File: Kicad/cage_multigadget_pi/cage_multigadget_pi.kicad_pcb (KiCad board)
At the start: 2 copper layers, 0.7 x 2.2 mm, 41 parts, among them J1 USB_B_Micro, J2 Raspberry_Pi_2_3, Q1 BSN20, Q2 BSN20, Q3 BSN20, Q4 BSN20, Q5 BSN20, U1 OP495, U2 MCP3004, U3 LED_shift_register_SPI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

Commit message: Updating the edges of the boards
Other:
- board size 0.7 x 2.2 mm -> 54.3 x 107.2 mm
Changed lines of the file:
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@@
-(kicad_pcb (version 20171130) (host pcbnew 5.1.4-e60b266~84~ubuntu18.04.1)
+(kicad_pcb (version 20171130) (host pcbnew 5.1.5-52549c5~84~ubuntu18.04.1)
   (general
     (thickness 1.6)
-    (drawings 3)
+    (drawings 7)
     (tracks 435)
     (zones 0)
@@
     )
   )
+  (gr_line (start 170.8531 51.6001) (end 116.5987 51.6001) (layer Edge.Cuts) (width 0.1))
+  (gr_line (start 170.8531 158.7881) (end 170.8531 51.6001) (layer Edge.Cuts) (width 0.1))
+  (gr_line (start 116.586 158.7881) (end 170.8531 158.7881) (layer Edge.Cuts) (width 0.1))
+  (gr_line (start 116.586 51.6001) (end 116.586 158.7881) (layer Edge.Cuts) (width 0.1))
   (gr_text "MULTIGADGET DEVICES" (at 153.6 140.3 90) (layer F.SilkS)
     (effects (font (size 1.5 1.5) (thickness 0.3)))
@@
   (segment (start 141.8 65.67863) (end 138.811372 62.690002) (width 0.25) (layer F.Cu) (net 11))
   (segment (start 141.8 66.81) (end 141.8 65.67863) (width 0.25) (layer F.Cu) (net 11))
-  (segment (start 122.559001 56.435001) (end 127.9906 61.8666) (width 0.25) (layer B.Cu) (net 43))
-  (segment (start 121.459001 56.435001) (end 122.559001 56.435001) (width 0.25) (layer B.Cu) (net 43) (status 10))
-  (via (at 127.9906 135.7249) (size 0.8) (drill 0.4) (layers F.Cu B.Cu) (net 43))
   (segment (start 121.506002 79.248) (end 121.459001 79.295001) (width 0.25) (layer F.Cu) (net 23) (status 30))
   (segment (start 126.311 79.248) (end 121.506002 79.248) (width 0.25) (layer F.Cu) (net 23) (status 30))
@@
   (segment (start 126.057 124.245) (end 126.558 124.746) (width 0.25) (layer F.Cu) (net 27) (status 20))
   (segment (start 126.057 121.158) (end 126.057 124.245) (width 0.25) (layer F.Cu) (net 27) (status 10))
+  (segment (start 122.559001 56.435001) (end 127.9906 61.8666) (width 0.25) (layer B.Cu) (net 43))
+  (segment (start 121.459001 56.435001) (end 122.559001 56.435001) (width 0.25) (layer B.Cu) (net 43) (status 10))
+  (via (at 127.9906 135.7249) (size 0.8) (drill 0.4) (layers F.Cu B.Cu) (net 43))
   (segment (start 129.286 82.246) (end 128.712 82.82) (width 0.25) (layer F.Cu) (net 43) (status 20))
   (segment (start 129.286 79.248) (end 129.286 82.246) (width 0.25) (layer F.Cu) (net 43) (status 10))

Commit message: added reward line, changed 2x40 pin header to 2x20 header, changed USB footprint and shifted
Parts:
- added J3: Reward, Socket_Strips:Socket_Strip_Straight_1x02_Pitch2.54mm, F.Cu at (143.5, 54.6)
- J1: footprint Connector_USB:USB_Micro-B_Amphenol_10103594-0001LF_Horizontal -> Digikey_footprints:USB_Micro_B_Female_10118194-0001LF
- J2: footprint Connector_PinSocket_2.54mm:PinSocket_2x40_P2.54mm_Vertical -> Pin_Headers:Pin_Header_Straight_2x20_Pitch2.54mm; moved to B.Cu
- moved J1 0.36 mm to (130.8, 57.1)
- moved J2 0.07 mm to (121.4, 56.4), turned to 180 degrees
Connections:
- J2 pad 11: Net-(J2-Pad11) -> /Reward
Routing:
- net /Reward: track 0.00 -> 38.7 mm
- net GND: track 181.4 -> 201.1 mm
- net Net-(J1-Pad6): track 10.6 -> 0.00 mm
- net +5V: track 278.4 -> 280.1 mm

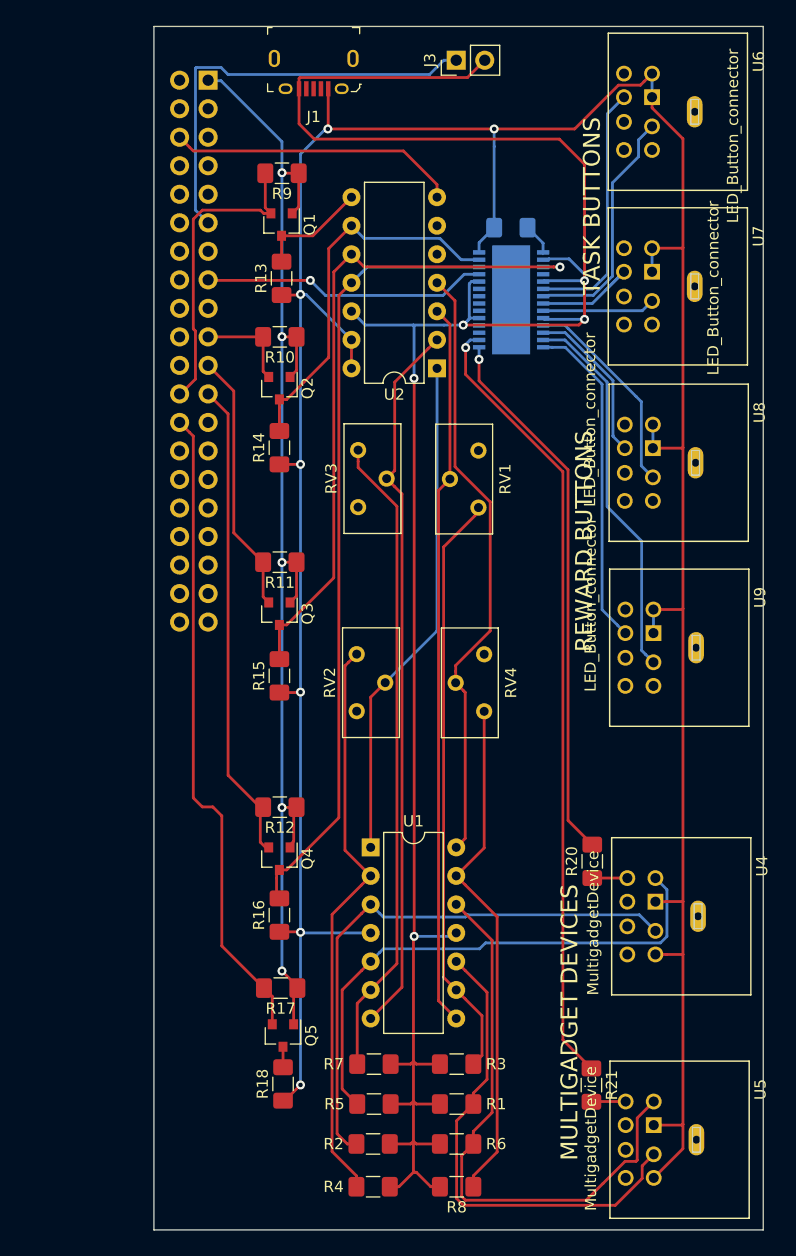
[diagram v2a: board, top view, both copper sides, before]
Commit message: changes to the multigadget circuit
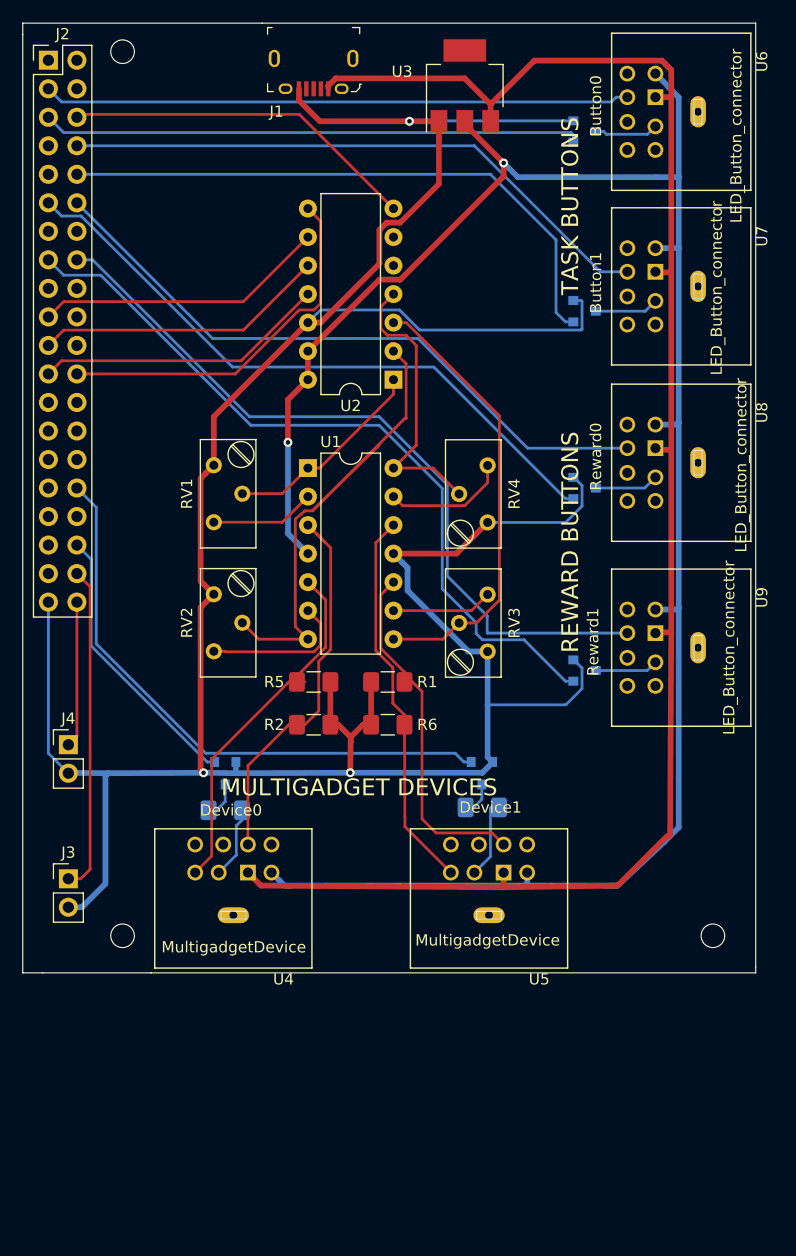
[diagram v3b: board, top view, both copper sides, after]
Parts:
- removed R10, R11, R12, R13, R14, R15, R16, R17, R18, R19, R9: 10k, Resistor_SMD:R_1206_3216Metric_Pad1.42x1.75mm_HandSolder
- removed R3, R4, R7, R8: 1k, Resistor_SMD:R_1206_3216Metric_Pad1.42x1.75mm_HandSolder
- added J4: Conn_01x02, Socket_Strips:Socket_Strip_Straight_1x02_Pitch2.54mm, F.Cu at (109.0, 115.6)
- added Q6: BSN20, TO_SOT_Packages_SMD:SOT-23, B.Cu at (154.9, 77.0)
- J2: moved to F.Cu
- J3: value Reward -> Conn_01x02
- Q1, Q2, Q3, Q4, Q5: footprint Package_TO_SOT_SMD:SOT-23 -> TO_SOT_Packages_SMD:SOT-23; moved to B.Cu
- R20, R21: moved to B.Cu
- RV1, RV2, RV3, RV4: footprint Potentiometer_THT:Potentiometer_Bourns_3296Y_Vertical -> Potentiometers:Potentiometer_Trimmer_Bourns_3296Y
- U3: value LED_shift_register_SPI -> AZ1117-3.3; footprint Package_SO:HTSSOP-28-1EP_4.4x9.7mm_P0.65mm_EP3.4x9.5mm_Mask2.4x6.17mm -> TO_SOT_Packages_SMD:SOT-223; moved to F.Cu
- moved Q5 84.9 mm to (154.9, 61.0), turned to 0 degrees
- moved J3 80.7 mm to (109.0, 127.5), turned to 0 degrees
- moved Q1 49.1 mm to (122.9, 118.1)
- moved Q2 38.7 mm to (145.8, 118.1)
- moved R1 38.1 mm to (137.4, 110.0)
- moved R5 38.0 mm to (130.8, 110.0)
- moved R6 37.8 mm to (137.4, 113.8)
- moved R2 37.7 mm to (130.8, 113.8)
- moved U4 36.4 mm to (125.0, 127.0), turned to 180 degrees
- moved U1 34.2 mm to (130.3, 90.9)
- moved R20 33.0 mm to (122.9, 121.4), turned to 180 degrees
- moved Q4 31.9 mm to (154.9, 109.0), turned to 0 degrees
- moved Q3 29.4 mm to (154.9, 92.7), turned to 0 degrees
- moved R21 26.6 mm to (145.8, 121.2), turned to 0 degrees
- moved U5 26.2 mm to (147.7, 127.0), turned to 180 degrees
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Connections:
- J2 pad 1: /3V_source -> Net-(J2-Pad1)
- J2 pad 10: Net-(J2-Pad10) -> /Button1LED
- J2 pad 11: /Reward -> /Reward0LED
- J2 pad 12: Net-(J2-Pad12) -> /Reward0Button
- J2 pad 15: /Reset -> /Reward1LED
- J2 pad 16: Net-(J2-Pad16) -> /Reward1Button
- J2 pad 19: /MOSI_3V -> /MOSI
- J2 pad 21: /MISO_3V -> /MISO
- J2 pad 23: /SCLK_3V -> /SCLK
- J2 pad 24: /Chip_Select_ADC_3V -> /Chip_Select_ADC
- J2 pad 26: /Chip_Select_LED_3V -> Net-(J2-Pad26)
- J2 pad 3: Net-(J2-Pad3) -> /Button0
- J2 pad 32: Net-(J2-Pad32) -> /Device1LED
- J2 pad 36: Net-(J2-Pad36) -> /Device0LED
- J2 pad 38: Net-(J2-Pad38) -> /Reward0
- J2 pad 39: Net-(J2-Pad39) -> GND
- J2 pad 40: Net-(J2-Pad40) -> /Reward1
- J2 pad 5: Net-(J2-Pad5) -> /Button0LED
- J2 pad 8: Net-(J2-Pad8) -> /Button1
- J3 pad 1: /Reward -> /Reward0
- Q1 pad 1: /3V_source -> /Device0LED
- Q1 pad 2: /Chip_Select_ADC_3V -> GND
- Q1 pad 3: /Chip_Select_ADC_5V -> Net-(Q1-Pad3)
- Q2 pad 1: /3V_source -> /Device1LED
- Q2 pad 2: /MOSI_3V -> GND
- Q2 pad 3: /MOSI_5V -> Net-(Q2-Pad3)
- Q3 pad 1: /3V_source -> /Reward0LED
- Q3 pad 2: /MISO_3V -> GND
- Q3 pad 3: /MISO_5V -> Net-(Q3-Pad3)
- Q4 pad 1: /3V_source -> /Reward1LED
- Q4 pad 2: /SCLK_3V -> GND
- Q4 pad 3: /SCLK_5V -> Net-(Q4-Pad3)
- Q5 pad 1: /3V_source -> /Button0LED
- Q5 pad 2: /Chip_Select_LED_3V -> GND
- Q5 pad 3: /Chip_Select__LED_5V -> Net-(Q5-Pad3)
- R20 pad 2: /Device0LED -> Net-(Q1-Pad3)
- R21 pad 1: /Device1LED -> Net-(Q2-Pad3)
- RV1 pad 1: Net-(R3-Pad1) -> GND
- RV2 pad 1: Net-(R4-Pad1) -> GND
- RV3 pad 1: Net-(R7-Pad1) -> GND
- RV4 pad 1: Net-(R8-Pad1) -> GND
- U1 pad 1: Net-(RV2-Pad2) -> Net-(RV1-Pad2)
- U1 pad 13: Net-(R8-Pad1) -> Net-(RV4-Pad3)
- U1 pad 2: Net-(R4-Pad1) -> Net-(RV1-Pad3)
- U1 pad 4: +5V -> +3V3
- U1 pad 6: Net-(R7-Pad1) -> Net-(RV2-Pad3)
- U1 pad 7: Net-(RV3-Pad2) -> Net-(RV2-Pad2)
- U1 pad 8: Net-(RV1-Pad2) -> Net-(RV3-Pad2)
- U1 pad 9: Net-(R3-Pad1) -> Net-(RV3-Pad3)
- U2 pad 1: Net-(RV2-Pad2) -> Net-(RV1-Pad2)
- U2 pad 10: /MISO_5V -> /MISO
- U2 pad 11: /SCLK_5V -> /SCLK
- U2 pad 13: +5V -> +3V3
- U2 pad 14: +5V -> +3V3
- U2 pad 2: Net-(RV3-Pad2) -> Net-(RV2-Pad2)
- U2 pad 3: Net-(RV1-Pad2) -> Net-(RV3-Pad2)
- U2 pad 8: /Chip_Select_ADC_5V -> /Chip_Select_ADC
- U2 pad 9: /MOSI_5V -> /MOSI
- U3 pad 1: Net-(R19-Pad2) -> GND
- U3 pad 2: GND -> +3V3
- U3 pad 3: /MISO_5V -> +5V
- U3 pad 4: /Chip_Select_LED_5V -> (no net)
- U4 pad 2: /Device0_FSR0 -> Net-(R20-Pad1)
- U4 pad 3: /Device0_FSR1 -> +3V3
- U4 pad 4: (no net) -> /Device0_FSR0
- U4 pad 5: +5V -> /Device0_FSR1
- U4 pad 6: Net-(R20-Pad1) -> (no net)
- U5 pad 2: /Device1_FSR0 -> Net-(R21-Pad2)
- U5 pad 3: /Device1_FSR1 -> +3V3
- U5 pad 4: (no net) -> /Device1_FSR0
- U5 pad 5: +5V -> /Device1_FSR1
- U5 pad 6: Net-(R21-Pad2) -> (no net)
- U6 pad 2: /ButtonLED0 -> Net-(Q5-Pad3)
- U6 pad 3: +5V -> +3V3
- U7 pad 2: /ButtonLED1 -> Net-(Q6-Pad3)
- U7 pad 3: +5V -> +3V3
- U8 pad 2: /RewardLED0 -> Net-(Q3-Pad3)
- U8 pad 3: +5V -> +3V3
- U8 pad 4: /RewardButton0 -> /Reward0Button
- U9 pad 2: /RewardLED1 -> Net-(Q4-Pad3)
- U9 pad 3: +5V -> +3V3
- U9 pad 4: /RewardButton1 -> /Reward1Button
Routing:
- net +3V3: track 0.00 -> 180.2 mm, vias 0 -> 2
- net +5V: track 280.1 -> 150.4 mm, vias 7 -> 0
- net /3V_source: track 108.5 -> 0.00 mm, vias 5 -> 0
- net /SCLK_5V: track 69.8 -> 0.00 mm
- net /Reward1Button: track 0.00 -> 68.4 mm
- net /Reward1LED: track 0.00 -> 68.1 mm
- net GND: track 201.1 -> 268.1 mm, vias 5 -> 3
- net /MISO_5V: track 59.7 -> 0.00 mm, vias 1 -> 0
- net /Reward0Button: track 0.00 -> 58.1 mm
- net /Reward0LED: track 0.00 -> 57.7 mm
- net Net-(R7-Pad1): track 57.6 -> 0.00 mm
- net /Chip_Select_LED_3V: track 57.5 -> 0.00 mm
- net /Button1LED: track 0.00 -> 53.4 mm
- net Net-(R3-Pad1): track 52.8 -> 0.00 mm
- net Net-(R4-Pad1): track 51.1 -> 0.00 mm
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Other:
- board size 54.3 x 107.2 mm -> 65.3 x 84.6 mm
- board text added: "Button0"
- board text added: "Button1"
- board text added: "Device0"
- board text added: "Device1"
- board text added: "Reward0"
- board text added: "Reward1"

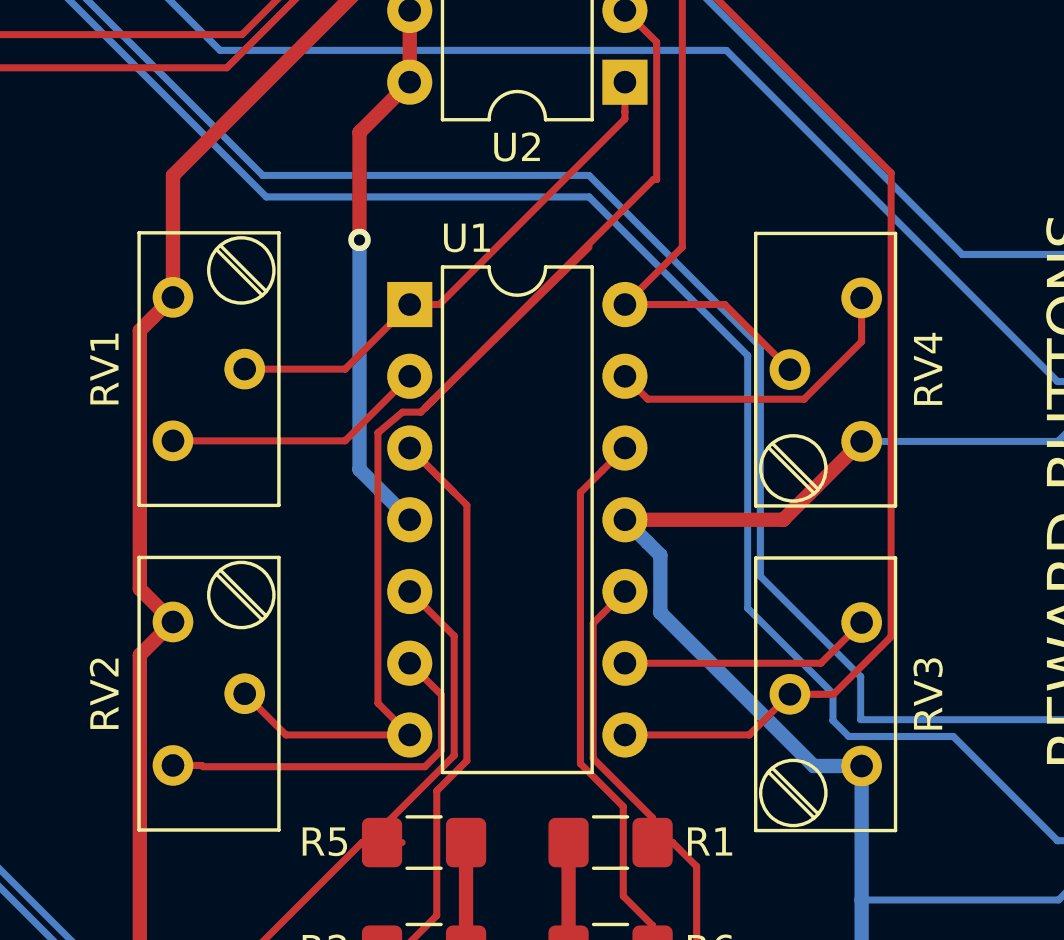
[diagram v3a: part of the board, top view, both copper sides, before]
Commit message: updating the amplifier gain setup to so that it's actually going to work...
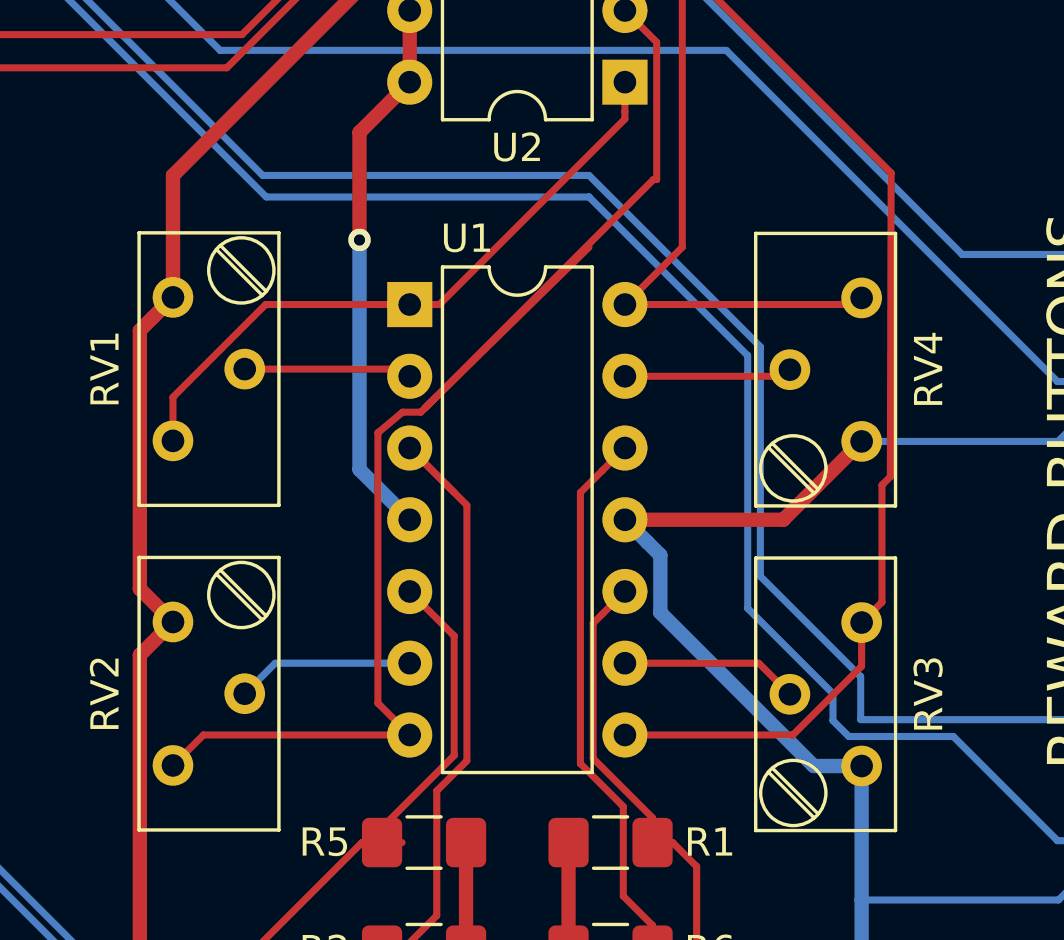
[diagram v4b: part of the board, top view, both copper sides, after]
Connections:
- U1 pad 1: Net-(RV1-Pad2) -> Net-(RV1-Pad3)
- U1 pad 13: Net-(RV4-Pad3) -> Net-(RV4-Pad2)
- U1 pad 14: Net-(RV4-Pad2) -> Net-(RV4-Pad3)
- U1 pad 2: Net-(RV1-Pad3) -> Net-(RV1-Pad2)
- U1 pad 6: Net-(RV2-Pad3) -> Net-(RV2-Pad2)
- U1 pad 7: Net-(RV2-Pad2) -> Net-(RV2-Pad3)
- U1 pad 8: Net-(RV3-Pad2) -> Net-(RV3-Pad3)
- U1 pad 9: Net-(RV3-Pad3) -> Net-(RV3-Pad2)
- U2 pad 1: Net-(RV1-Pad2) -> Net-(RV1-Pad3)
- U2 pad 2: Net-(RV2-Pad2) -> Net-(RV2-Pad3)
- U2 pad 3: Net-(RV3-Pad2) -> Net-(RV3-Pad3)
- U2 pad 4: Net-(RV4-Pad2) -> Net-(RV4-Pad3)
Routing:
- net Net-(RV2-Pad2): track 45.8 -> 6.29 mm
- net Net-(RV2-Pad3): track 13.3 -> 48.1 mm
- net Net-(RV3-Pad2): track 40.2 -> 6.30 mm
- net Net-(RV3-Pad3): track 8.98 -> 40.1 mm
- net Net-(RV4-Pad2): track 25.9 -> 5.94 mm
- net Net-(RV4-Pad3): track 11.1 -> 27.6 mm
- net Net-(RV1-Pad3): track 9.33 -> 22.9 mm
- net Net-(RV1-Pad2): track 18.4 -> 5.95 mm
